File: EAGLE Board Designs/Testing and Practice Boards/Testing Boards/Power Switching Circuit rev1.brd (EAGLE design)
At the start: 93.1 x 66.3 mm, 52 parts, among them J1 CONNECTOR-3_, J2 CONNECTOR-4_SOURIAU_, J3 CONNECTOR-4_SOURIAU_, K1 J115F11A6*, Q1 SIR638ADP, Q2 SIR638ADP, Q3 SIR638ADP, Q4 SIR638ADP, U1 LTC4421

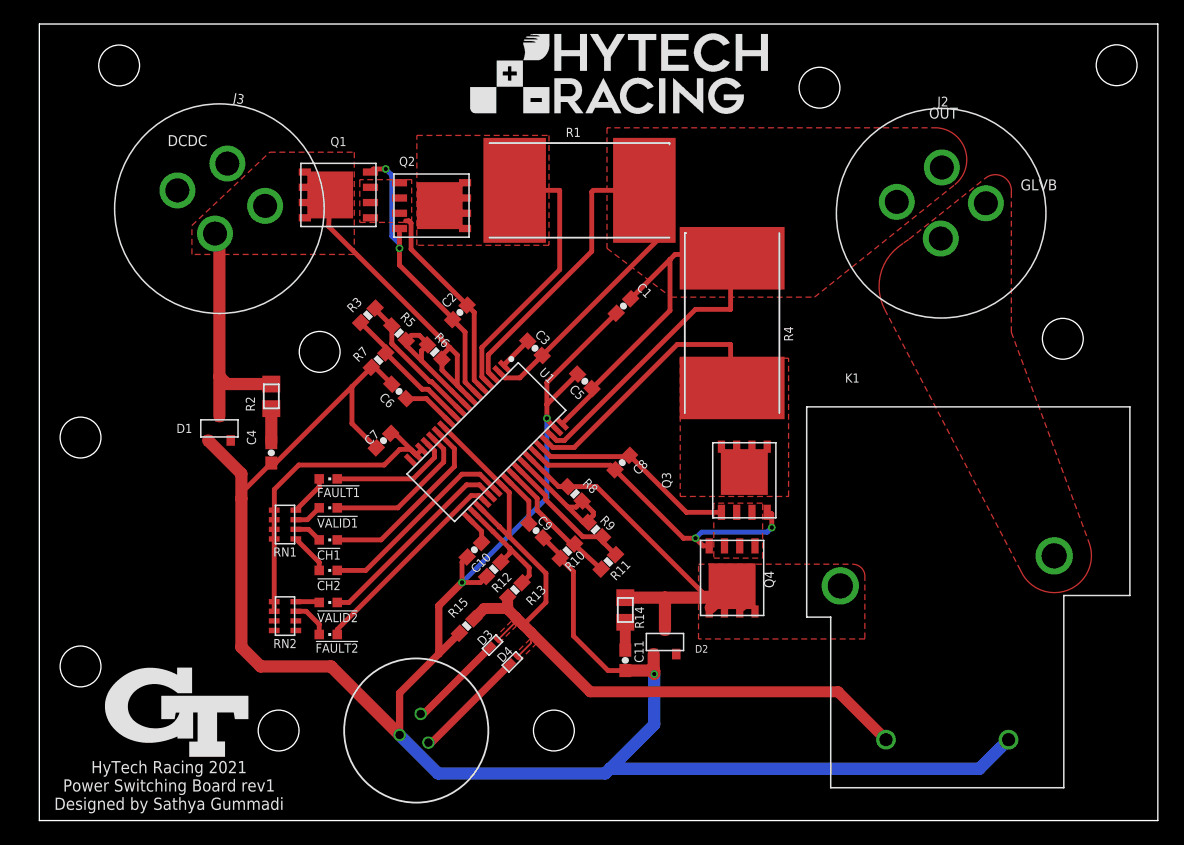
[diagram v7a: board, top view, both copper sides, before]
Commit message: FIxed routing to remove clearance errors
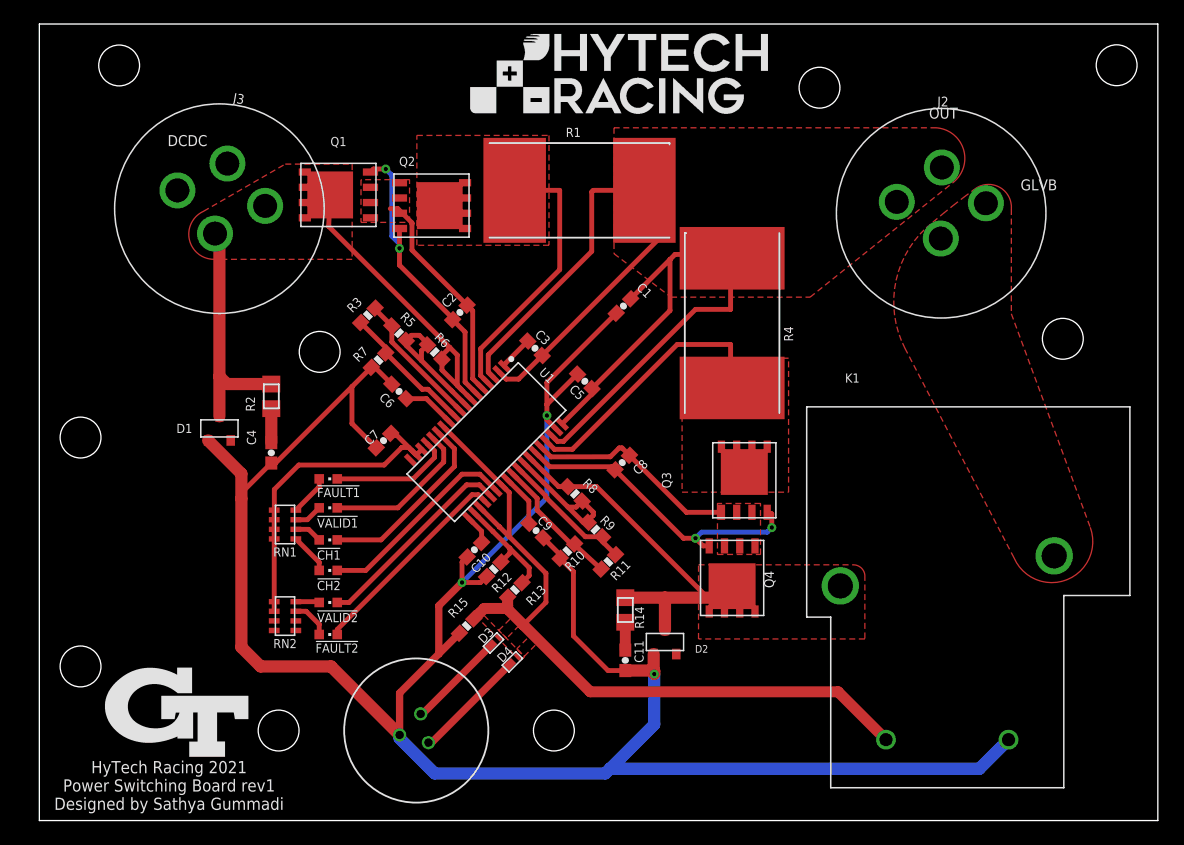
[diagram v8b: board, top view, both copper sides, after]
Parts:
- moved D3 0.19 mm to (9.86, -12.0)
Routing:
- net RELAY: track 36.6 -> 30.9 mm
- net !SHDN!: track 69.6 -> 64.8 mm
- net SOURCE1: track 16.8 -> 18.5 mm
- net SENSE2: track 24.4 -> 23.0 mm
- net SOURCE2: track 17.5 -> 18.2 mm
